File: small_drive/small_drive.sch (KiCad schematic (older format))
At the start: 159 parts, among them J1 DB9, J2 DB15, M1 SiR826DP, M2 SiR826DP, M3 SiR826DP, M4 SiR826DP, M5 SiR826DP, M6 SiR826DP, P1 CONN_01X04, P2 CONN_01X04, P3 CONN_01X04, P4 CONN_01X04, P5 CONN_01X02, P6 CONN_01X02, P7 CONN_01X02, P8 CONN_01X01, U1 XMC4400-F64x512, U10 LM5106, U11 ACS711KLCTR-12AB-T, U12 ACS711ELCTR-25AB-T, U13 ACS711KLCTR-12AB-T, U14 AD8226, U15 MAX3096, U16 AMC1203, U17 7805, U18 LT1764EQ, U19 KSZ8081, U2 ips511g, U20 ETH100_MAG, U3 ips511g, U4 LTC2850, U5 AD8226, U6 LT1764EQ, U7 MC33074DTBR2, U8 LM5106, U9 LM5106, X1 NKE1212DC, X2 NKE1212DC, X3 HCPL0201, X4 HCPL0201, X5 HCPL0201, X6 HCPL0201, Y1 12MHz, Y2 25MHz

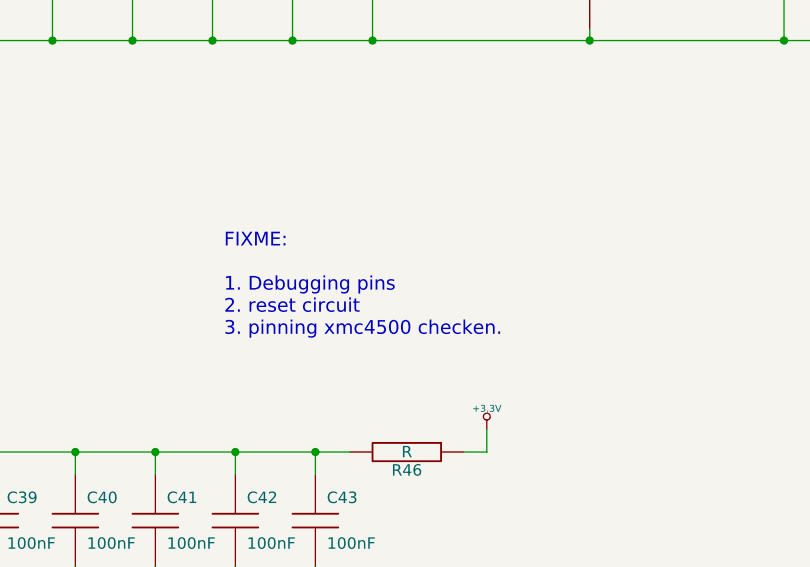
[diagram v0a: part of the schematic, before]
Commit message: Adding timestamp. Fixed port numbers.
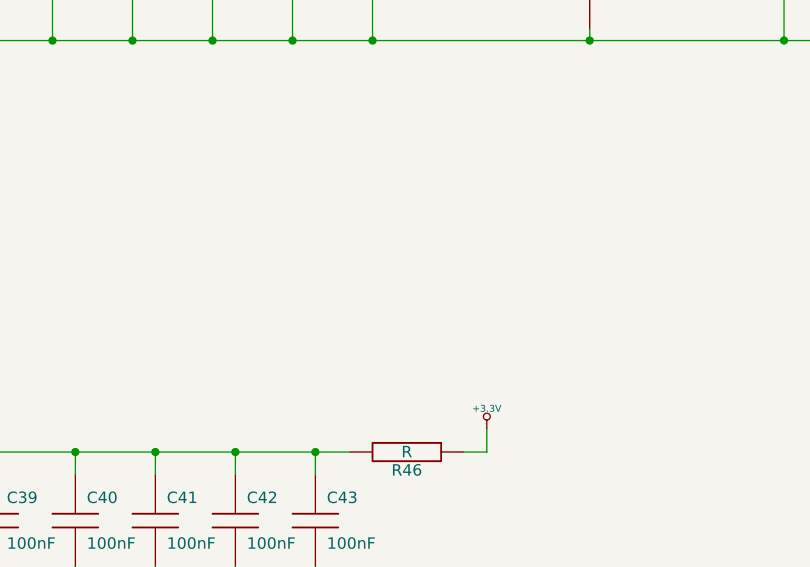
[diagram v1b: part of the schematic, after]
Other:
- note removed: "FIXME:\n\n1. Debugging pins\n2. reset circuit\n3. pinning xmc4500 checken.\n"
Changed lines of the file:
@@
 	1    0    0    1
 $EndComp
-Text Notes 7400 3250 0    60   ~ 0
-FIXME:\n\n1. Debugging pins\n2. reset circuit\n3. pinning xmc4500 checken.\n
 $Comp
 L XMC4400-F64x512 U1

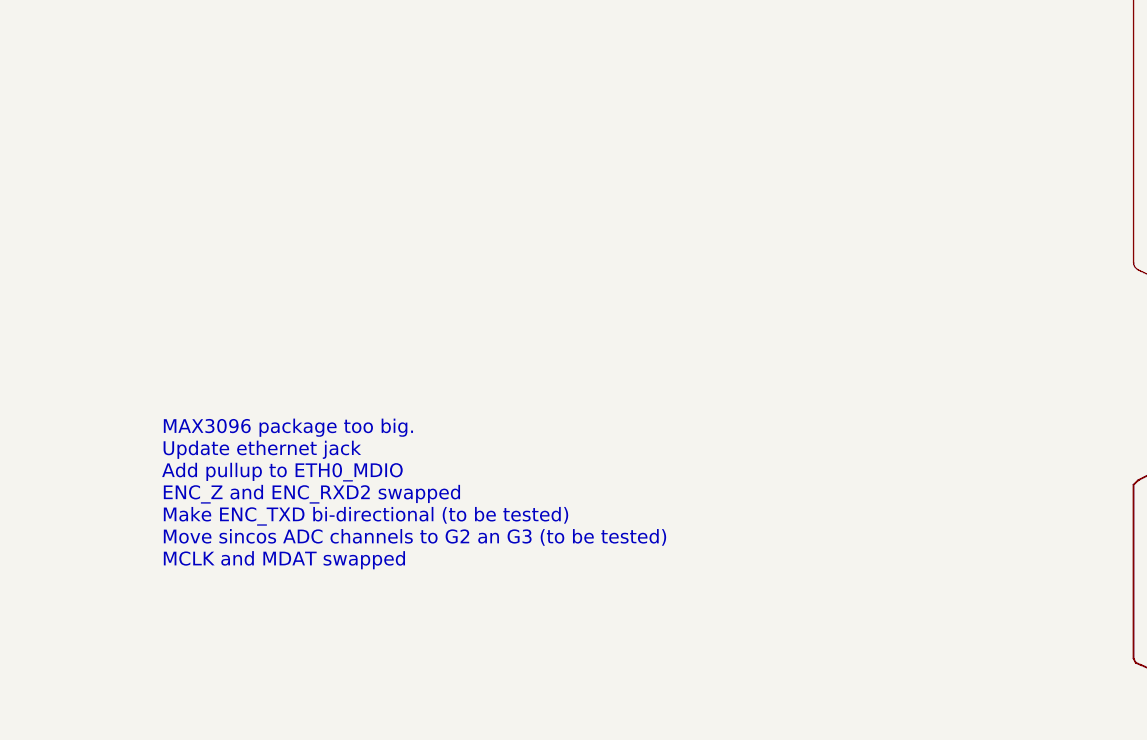
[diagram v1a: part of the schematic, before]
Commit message: Hiperface interpolation (needs hardware patches)
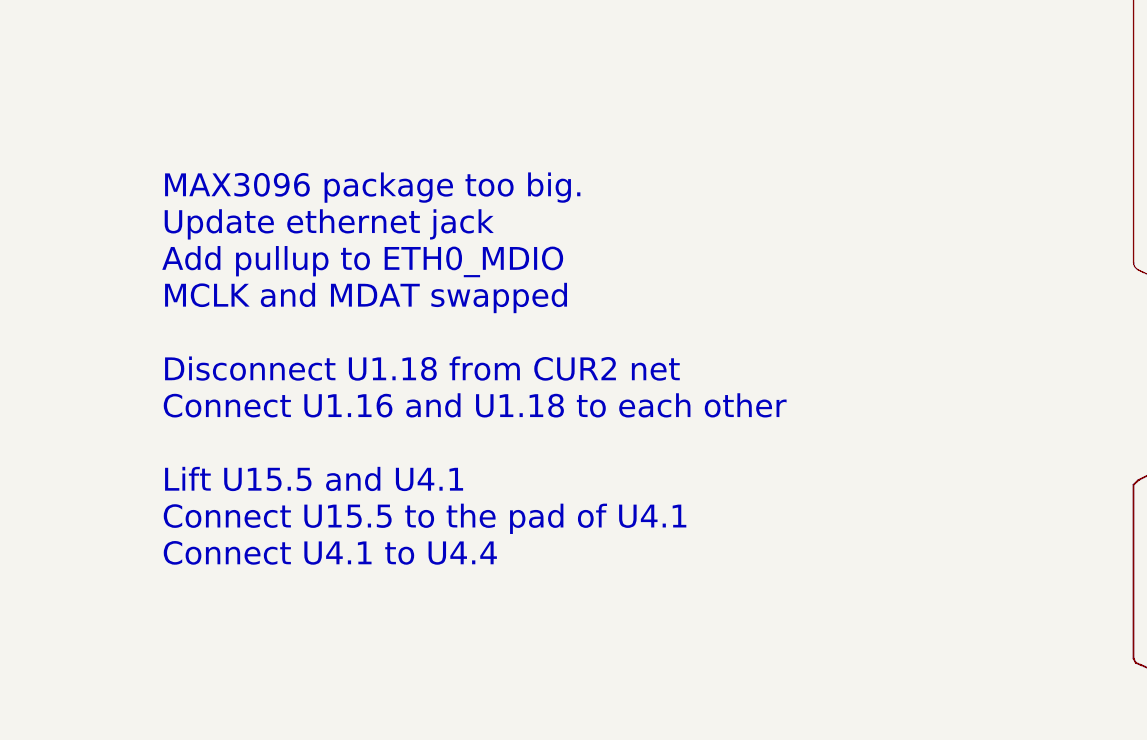
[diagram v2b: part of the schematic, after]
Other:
- note added: "MAX3096 package too big.\nUpdate ethernet jack\nAdd pullup to ETH0_MDIO\nMCLK and MDAT swapped\n\nDisconnect U1.18 from CUR2 net\nConnect U1.16 and U1.18 to each other\n\nLift U15.5 and U4.1\nConnect U15.5 to the pad of U4.1\nConnect U4.1 to U4.4"
- note removed: "MAX3096 package too big.\nUpdate ethernet jack\nAdd pullup to ETH0_MDIO\nENC_Z and ENC_RXD2 swapped\nMake ENC_TXD bi-directional (to be tested)\nMove sincos ADC channels to G2 an G3 (to be tested)\nMCLK and MDAT swapped"
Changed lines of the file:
@@
 Text Label 2600 9600 0    60   ~ 0
 SWCLK
-Text Notes 4950 14000 0    60   ~ 0
-MAX3096 package too big.\nUpdate ethernet jack\nAdd pullup to ETH0_MDIO\nENC_Z and ENC_RXD2 swapped\nMake ENC_TXD bi-directional (to be tested)\nMove sincos ADC channels to G2 an G3 (to be tested)\nMCLK and MDAT swapped
+Text Notes 4950 14000 0    100  ~ 0
+MAX3096 package too big.\nUpdate ethernet jack\nAdd pullup to ETH0_MDIO\nMCLK and MDAT swapped\n\nDisconnect U1.18 from CUR2 net\nConnect U1.16 and U1.18 to each other\n\nLift U15.5 and U4.1\nConnect U15.5 to the pad of U4.1\nConnect U4.1 to U4.4
 Text Label 10100 12400 0    60   ~ 0
 ENC_TXN

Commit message: Fully routed PCB with 100-pin package
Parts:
- removed U1: XMC4400-F64x512, Housings_QFP:LQFP-64-1EP_10x10mm_Pitch0.5mm, symbol XMC4400-F64x512
- removed U15: MAX3096, Housings_SOIC:SOIC-16_3.9x9.9mm_Pitch1.27mm, symbol MAX3096
- removed U7: MC33074DTBR2, Housings_SSOP:TSSOP-14_4.4x5mm_Pitch0.65mm, symbol MC33074DTBR2
- added R49, R53, R54, R55, R58, R59: 1k, Resistors_SMD:R_0603, symbol R-RESCUE-small_drive
- added R50, R51, R52, R56, R57: 510, Resistors_SMD:R_0603, symbol R-RESCUE-small_drive
- added U1: XMC4400-F100, Housings_QFP:TQFP-100-1EP_14x14mm_Pitch0.5mm, symbol XMC4400-F100
- added U15, U21, U22, U23: MAX3463, Housings_SOIC:SOIC-8_3.9x4.9mm_Pitch1.27mm, symbol LTC2850-RESCUE-small_drive
- added U7: MC33074DTBR2, Housings_SSOP:TSSOP-14_4.4x5mm_Pitch0.65mm, symbol TL074
- C10, C11, C12, C13, C15, C16, C17, C18, C19, C20, C21, C22, C23, C24, C25, C26, C27, C28, C29, C3, C30, C31, C33, C35, C37, C39, C40, C41, C42, C43, C44, C45, C46, C47, C48, C49, C50, C51, C52, C53, C54, C55, C56, C57, C58, C59, C7, C8, C9: symbol C -> C-RESCUE-small_drive
- J1: footprint Connectors_Amphenol:DB9FC_HD-20 -> 00_Passives:DB9F_ebay
- J2: footprint Connectors_Amphenol:DB15F_HD20_SIZE2 -> 00_Passives:DB15F_ebay
- R1, R10, R11, R12, R13, R14, R15, R16, R17, R18, R19, R2, R20, R21, R22, R23, R24, R25, R26, R27, R28, R29, R3, R30, R31, R32, R33, R34, R35, R36, R37, R38, R39, R4, R40, R41, R42, R43, R44, R45, R46, R47, R48, R5, R6, R7, R8, R9: symbol R -> R-RESCUE-small_drive
- U12: value ACS711ELCTR-25AB-T -> ACS711ELCTR-12AB-T
- U13: PartNr ACS711ELCTR-25AB-T -> ACS711ELCTR-12AB-T
- U4: value LTC2850 -> MAX3463; digikey LTC2850IS8#PBF-ND -> (none)
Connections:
- net labels added: ENC0_DIR, ENC0_RXD, ENC0_TXD, ENC1_A/DATA, ENC1_B/CLK, ENC1_CDIR, ENC1_DDIR, ENC1_Z/SELECT, ETH0_CLK_RMII, ETH0_CRS_DV, ETH0_INT, ETH0_RXD0, ETH0_RXD1, ETH0_RXER
- net labels removed: ENC_A, ENC_B, ENC_DIR, ENC_RXD, ENC_RXD2, ENC_TXD, ENC_Z, ETH0_CLK_RMIIA, ETH0_RXD0A, ETH0_RXD1A, ETH0_RXERA, ETH_CRS_DVA
- wire segments 666 -> 716
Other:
- note added: "MAX3096 package too big.\nUpdate ethernet jack\nDisconnect U1.18 from CUR2 net\nConnect U1.16 and U1.18 to each other\n\nLift U15.5 and U4.1\nConnect U15.5 to the pad of U4.1\nConnect U4.1 to U4.4"
- note added: "P14.12 VADC_G1CH1\nP14.7 POSIF0_IN0B\nP14.6 POSIF0_IN1B VADC_G0CH6"
- note added: "P14.4 VADC_G0CH4 VADC_G2CH0"
- note added: "P14.8 VADC_G1CH0 VADC_G3CH2"
- note added: "P15.3 VADC_G2CH3"
- note added: "P2.5 POSIF1_IN0A, U0C1_DOUT0, U0C1_DX0B\nP2.4 POSIF1_IN1A, U0C1_SCLKOUT, U0C1_DX1A\nP2.3 POSIF1_IN2A, U0C1_SELO0, U0C1_DX2A"
- note removed: "MAX3096 package too big.\nUpdate ethernet jack\nAdd pullup to ETH0_MDIO\nMCLK and MDAT swapped\n\nDisconnect U1.18 from CUR2 net\nConnect U1.16 and U1.18 to each other\n\nLift U15.5 and U4.1\nConnect U15.5 to the pad of U4.1\nConnect U4.1 to U4.4"
- note removed: "P0.1 ETH0 CRS_DVB\nP0.0 U1C1 DX0D\nP14.14 VADC G1CH6\nP14.7 VADC G0CH7 POSIF0 IN0B\nP14.6 VADC G0CH6 POSIF0 IN1B"
- note removed: "P1.3 POSIF0 IN0A\nP1.2 POSIF0 IN1A\nP1.1 POSIF0 IN2A\nP1.8 DSD MCLK1\nP0.6 HRPWM0 HROUT30\nP0.5 HRPWM0 HROUT00\nP0.3 HRPWM0 HROUT20"
- note removed: "P14.4 VADC G2CH0\nP14.0 VADC G0CH0\nP14.8 VADC G1CH0\nP2.9 ETH0 TXD1\nP2.8 ETH0 TXD0\nP2.5 ETH0 TX_EN\nP2.4 ETH0 RXERA\nP2.3 ETH0 RXD1A\nP2.2 ETH0 RXD0A"
- note removed: "P2.1 ETH0_CLKRMIIA\nP2.0 ETH0_MDO MDIB\nP2.7 ETH0_MDC\nP2.6 DSD_IN1B\nP1.5 U0C0_DOUT0\nP1.4 U0C0_DX0B"
- note removed: "Using POSIF_0B and ADC_G[01]CH6"
- moved on the sheet: C10, C11, C28, C29, C30, C31, C38, C39, C40, C41, C42, C43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

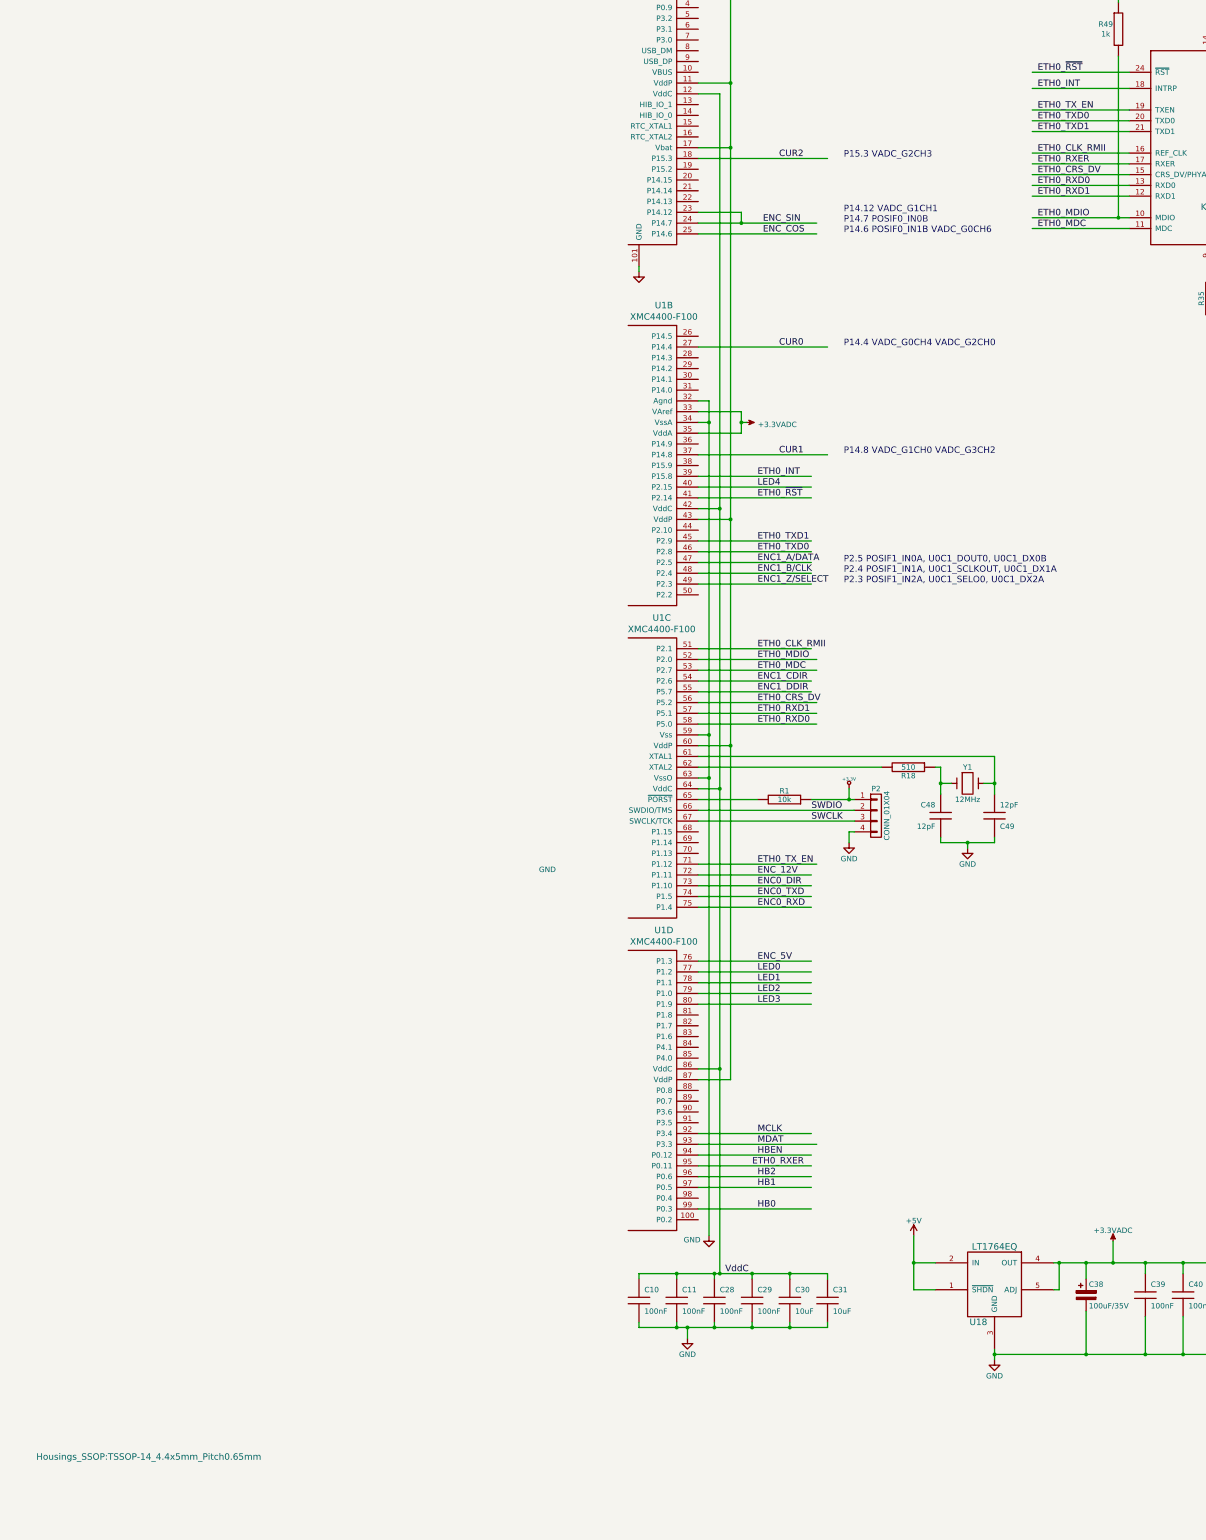
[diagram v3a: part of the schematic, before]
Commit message: New small_drive, untested, unverified.
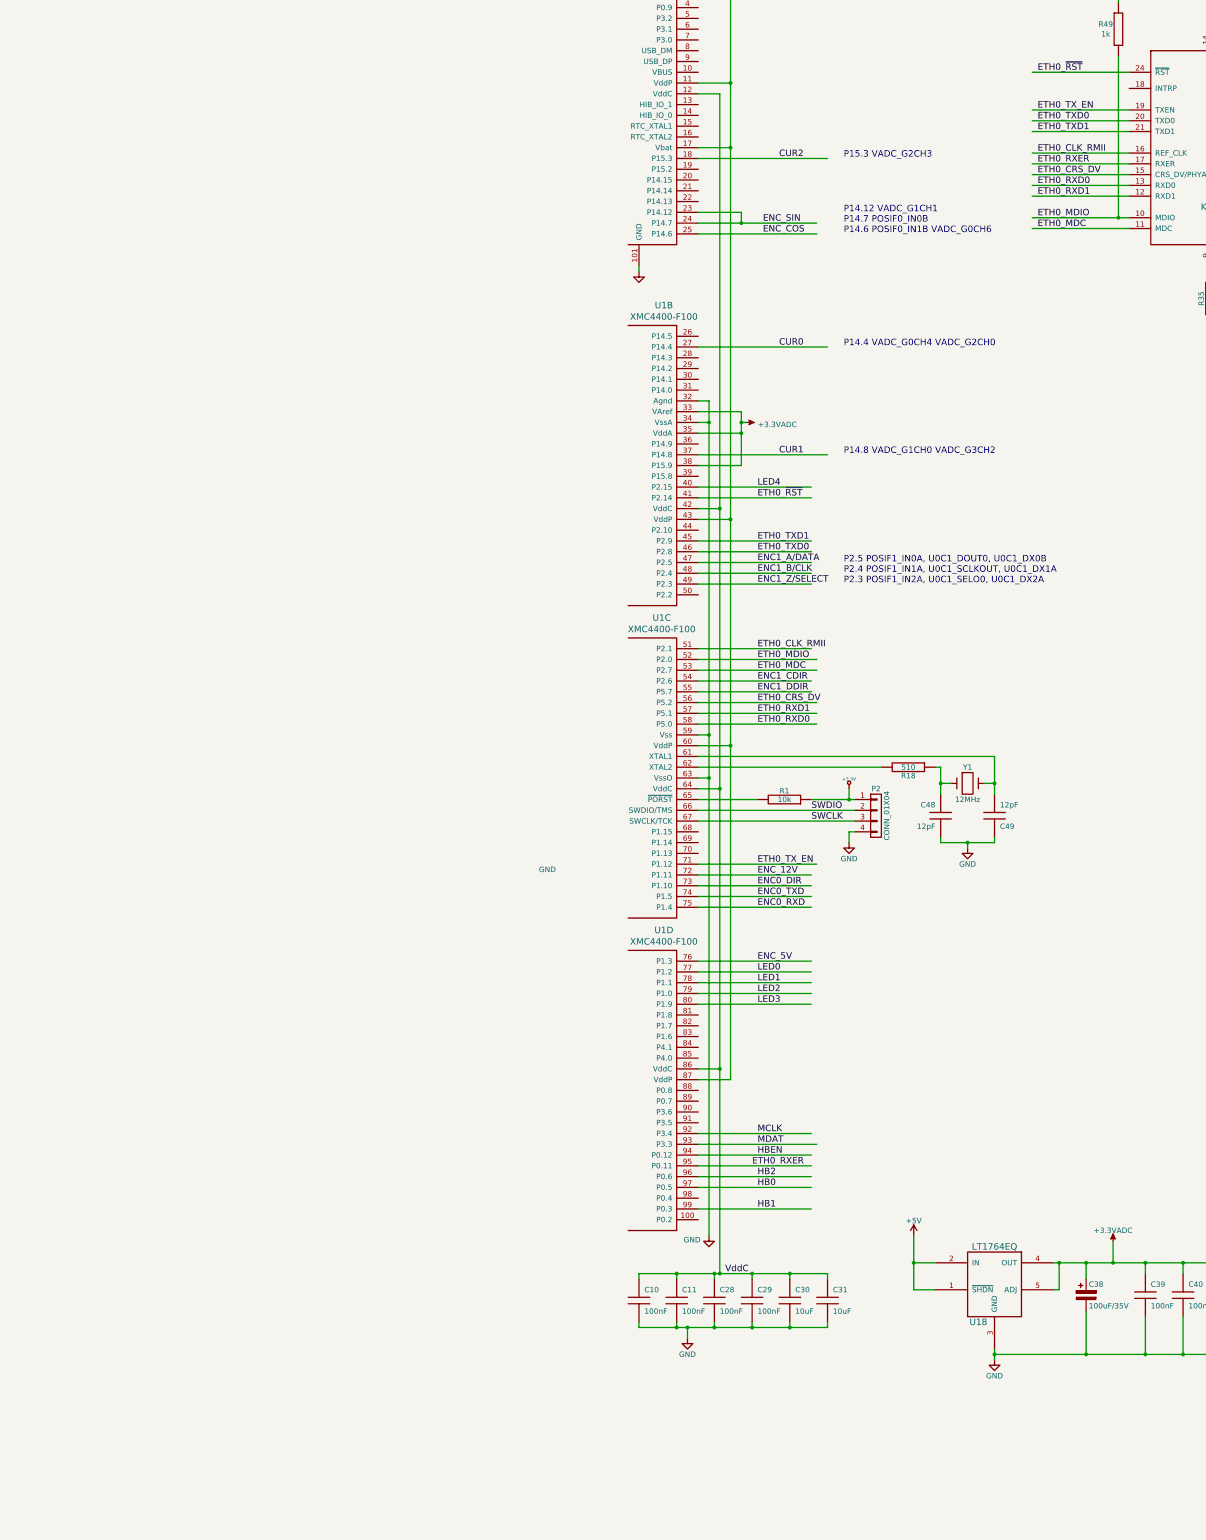
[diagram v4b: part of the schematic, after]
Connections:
- net labels removed: ETH0_INT
- wire segments 716 -> 715
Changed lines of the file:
@@
 Text Label 15450 6100 0    60   ~ 0
 CUR0
-Text Label 1800 13800 0    60   ~ 0
+Text Label 1800 14000 0    60   ~ 0
 HB1
 Text Label 1800 13700 0    60   ~ 0
@@
 Text Label 1800 10800 0    60   ~ 0
 ETH0_TX_EN
-Text Label 1800 14000 0    60   ~ 0
+Text Label 1800 13800 0    60   ~ 0
 HB0
 Text Label 1800 8200 0    60   ~ 0
@@
 	1250 6600 1650 6600
 Wire Wire Line
-	1650 6600 1650 6800
+	1650 6600 1650 7100
 Wire Wire Line
 	1350 6500 1250 6500
@@
 Wire Wire Line
 	1250 9100 2300 9100
-Text Label 4400 3600 0    60   ~ 0
-ETH0_INT
-Wire Wire Line
-	4350 3600 5250 3600
-Text Label 1800 7200 0    60   ~ 0
-ETH0_INT
-Wire Wire Line
-	1250 7200 2300 7200
 $Comp
 L GND #PWR086
@@
 F 0 "U7" H 13000 6900 60  0000 C CNN
 F 1 "MC33074DTBR2" H 12700 6800 50  0000 L CNN
-F 2 "Housings_SSOP:TSSOP-14_4.4x5mm_Pitch0.65mm" H -3850 -2200 60  0000 C CNN
+F 2 "Housings_SSOP:TSSOP-14_4.4x5mm_Pitch0.65mm" H -3850 -2200 60  0001 C CNN
 F 3 "" H -3850 -2200 60  0000 C CNN
 	2    12700 7050
@@
 Wire Wire Line
 	700  5300 700  5250
+Wire Wire Line
+	1650 7100 1250 7100
+Connection ~ 1650 6800
 $EndSCHEMATC

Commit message: Adding more advanced speed observer model.
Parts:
- added C60, C61: 100nF, Capacitors_SMD:C_0603, symbol C-RESCUE-small_drive
- U1: symbol XMC4400-F100 -> XMC4400-F100-RESCUE-small_drive
- U7: symbol TL074 -> TL074-RESCUE-small_drive
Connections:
- wire segments 715 -> 721
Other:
- moved on the sheet: C12, C13, C14, C15, C16, C17, C18, C32, C33, C56, C57, C58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

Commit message: Use 5V for opamp supply.
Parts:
- added C62: 100nF, Capacitors_SMD:C_0603, symbol C-RESCUE-small_drive
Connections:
- wire segments 721 -> 717
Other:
- note removed: "MAX3096 package too big.\nUpdate ethernet jack\nDisconnect U1.18 from CUR2 net\nConnect U1.16 and U1.18 to each other\n\nLift U15.5 and U4.1\nConnect U15.5 to the pad of U4.1\nConnect U4.1 to U4.4"
- moved on the sheet: R10, R11, R12, R13, R14, R6, R7, R8, R9, U7A, U7C, U7D
